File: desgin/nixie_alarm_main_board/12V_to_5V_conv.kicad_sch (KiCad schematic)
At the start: 8 parts

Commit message: filter caps
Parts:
- added C5: 100nF 25V, GRM033D70J224ME01D, symbol SamacSys_Parts:GRM033R71E101KA01J
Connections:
- net +12V: now also C5.1
- net GND: now also C5.2
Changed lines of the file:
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@@
+	)
+	(junction
+		(at 85.09 73.152)
+		(diameter 0)
+		(color 0 0 0 0)
 	)
 	(junction
@@
 	(wire
 		(pts
-			(xy 94.742 73.152) (xy 101.854 73.152)
+			(xy 74.676 73.152) (xy 85.09 73.152)
 		)
 		(stroke
@@
 	(wire
 		(pts
+			(xy 85.09 75.438) (xy 85.09 73.152)
+		)
+		(stroke
+			(width 0)
+			(type default)
+		)
+	)
+	(wire
+		(pts
 			(xy 191.516 91.44) (xy 191.516 108.458)
 		)
@@
 		(pts
 			(xy 125.984 83.82) (xy 139.7 83.82)
+		)
+		(stroke
+			(width 0)
+			(type default)
+		)
+	)
+	(wire
+		(pts
+			(xy 85.09 73.152) (xy 101.854 73.152)
 		)
 		(stroke
@@
 	(hierarchical_label "+12V"
 		(shape input)
-		(at 94.742 73.152 180)
+		(at 74.676 73.152 180)
 		(fields_autoplaced yes)
 		(effects
@@
 		(fields_autoplaced yes)
 		(property "Reference" "R6"
-			(at 104.394 99.3139 90)
+			(at 104.14 99.3139 90)
 			(effects
 				(font
@@
 		)
 		(property "Value" "15kΩ"
-			(at 104.394 101.8539 90)
+			(at 104.14 101.8539 90)
 			(effects
 				(font
@@
 					(unit 1)
 				)
+			)
+		)
+	)
+	(symbol
+		(lib_id "power:GND")
+		(at 85.09 88.138 0)
+		(unit 1)
+		(exclude_from_sim no)
+		(in_bom yes)
+		(on_board yes)
+		(dnp no)
+		(fields_autoplaced yes)
+		(property "Reference" "#PWR017"
+			(at 85.09 94.488 0)
+			(effects
+				(font
+					(size 1.27 1.27)
+				)
+				(hide yes)
+			)
+		)
+		(property "Value" "GND"
+			(at 85.09 92.71 0)
+			(effects
+				(font
+					(size 1.27 1.27)
+				)
+			)
+		)
+		(property "Footprint" ""
+			(at 85.09 88.138 0)
+			(effects
+				(font
+					(size 1.27 1.27)
+				)
+				(hide yes)
+			)
+		)
+		(property "Datasheet" ""
+			(at 85.09 88.138 0)
+			(effects
+				(font
+					(size 1.27 1.27)
+				)
+				(hide yes)
+			)
+		)
+		(property "Description" "Power symbol creates a global label with name \"GND\" , ground"
+			(at 85.09 88.138 0)
+			(effects
+				(font
+					(size 1.27 1.27)
+				)
+				(hide yes)
+			)
+		)
+		(pin "1"
+		)
+		(instances
+			(project "nixie_alarm_main_board"
+				(path "/a0d555d7-39a0-4a98-b831-70d97d0aa5a1/0943c442-6dd2-4b0d-a6a3-5c379f0041bb"
+					(reference "#PWR017")
+					(unit 1)
+				)
+			)
+		)
+	)
+	(symbol
+		(lib_id "SamacSys_Parts:GRM033R71E101KA01J")
+		(at 85.09 75.438 270)
+		(unit 1)
+		(exclude_from_sim no)
+		(in_bom yes)
+		(on_board yes)
+		(dnp no)
+		(property "Reference" "C5"
+			(at 90.678 79.756 90)
+			(effects
+				(font
+					(size 1.27 1.27)
+				)
+				(justify right)
+			)
+		)
+		(property "Value" "100nF 25V"
+			(at 98.552 81.788 90)
+			(effects
+				(font
+					(size 1.27 1.27)
+				)
+				(justify right)
+			)
+		)
+		(property "Footprint" "GRM033D70J224ME01D"
+			(at -11.1 84.328 0)
+			(effects
+				(font
+					(size 1.27 1.27)
+				)
+				(justify left top)
+				(hide yes)
+			)
+		)
+		(property "Datasheet" "https://search.murata.co.jp/Ceramy/image/img/A01X/G101/ENG/GRM033R71E101KA01-01A.pdf"
+			(at -111.1 84.328 0)
+			(effects
+				(font
+					(size 1.27 1.27)
+				)
+				(justify left top)
+				(hide yes)
+			)
+		)
+		(property "Description" "Multilayer Ceramic Capacitors MLCC - SMD/SMT 100pF 25 volts 10%"
+			(at 85.09 75.438 0)
+			(effects
+				(font
+					(size 1.27 1.27)
+				)
+				(hide yes)
+			)
+		)
+		(property "Height" "0.5"
+			(at -311.1 84.328 0)
+			(effects
+				(font
+					(size 1.27 1.27)
+				)
+				(justify left top)
+				(hide yes)
+			)
+		)
+		(property "Mouser Part Number" "81-GRM033R71E101KA1J"
+			(at -411.1 84.328 0)
+			(effects
+				(font
+					(size 1.27 1.27)
+				)
+				(justify left top)
+				(hide yes)
+			)
+		)
+		(property "Mouser Price/Stock" "https://www.mouser.co.uk/ProductDetail/Murata-Electronics/GRM033R71E101KA01J?qs=563MOeNa05Lmru4oTW10Jw%3D%3D"
+			(at -511.1 84.328 0)
+			(effects
+				(font
+					(size 1.27 1.27)
+				)
+				(justify left top)
+				(hide yes)
+			)
+		)
+		(property "Manufacturer_Name" "Murata Electronics"
+			(at -611.1 84.328 0)
+			(effects
+				(font
+					(size 1.27 1.27)
+				)
+				(justify left top)
+				(hide yes)
+			)
+		)
+		(property "Manufacturer_Part_Number" "GRM033R71E101KA01J"
+			(at -711.1 84.328 0)
+			(effects
+				(font
+					(size 1.27 1.27)
+				)
+				(justify left top)
+				(hide yes)
+			)
+		)
+		(pin "1"
+		)
+		(pin "2"
+		)
+		(instances
+			(project "nixie_alarm_main_board"
+				(path "/a0d555d7-39a0-4a98-b831-70d97d0aa5a1/0943c442-6dd2-4b0d-a6a3-5c379f0041bb"
+					(reference "C5")
+					(unit 1)
+				)

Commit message: new rezistors
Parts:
- C3, C5: footprint GRM033D70J224ME01D -> Capacitor_SMD:C_0805_2012Metric_Pad1.18x1.45mm_HandSolder
- R1, R2, R5, R6: footprint ERJUP6 -> Resistor_SMD:R_0805_2012Metric_Pad1.20x1.40mm_HandSolder
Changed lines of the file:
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@@
 			)
 		)
-		(property "Footprint" "ERJUP6"
+		(property "Footprint" "Resistor_SMD:R_0805_2012Metric_Pad1.20x1.40mm_HandSolder"
 			(at 5.664 87.122 0)
 			(effects
@@
 			)
 		)
-		(property "Footprint" "ERJUP6"
+		(property "Footprint" "Resistor_SMD:R_0805_2012Metric_Pad1.20x1.40mm_HandSolder"
 			(at 61.036 104.648 0)
 			(effects
@@
 			)
 		)
-		(property "Footprint" "ERJUP6"
+		(property "Footprint" "Resistor_SMD:R_0805_2012Metric_Pad1.20x1.40mm_HandSolder"
 			(at 61.036 77.47 0)
 			(effects
@@
 			)
 		)
-		(property "Footprint" "ERJUP6"
+		(property "Footprint" "Resistor_SMD:R_0805_2012Metric_Pad1.20x1.40mm_HandSolder"
 			(at 5.664 105.664 0)
 			(effects
@@
 			)
 		)
-		(property "Footprint" "GRM033D70J224ME01D"
+		(property "Footprint" "Capacitor_SMD:C_0805_2012Metric_Pad1.18x1.45mm_HandSolder"
 			(at -11.1 84.328 0)
 			(effects
@@
 			)
 		)
-		(property "Footprint" "GRM033D70J224ME01D"
+		(property "Footprint" "Capacitor_SMD:C_0805_2012Metric_Pad1.18x1.45mm_HandSolder"
 			(at 287.706 82.55 0)
 			(effects

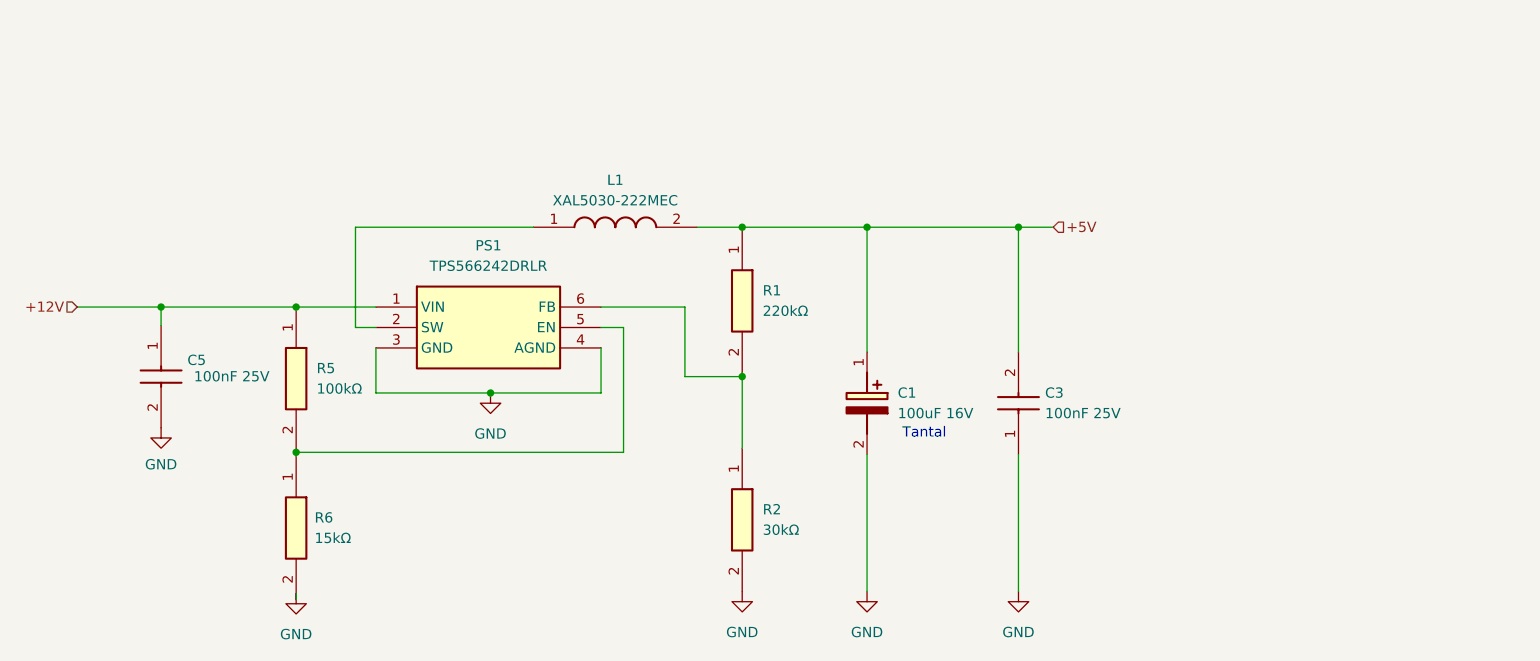
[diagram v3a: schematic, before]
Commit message: traces for nixie tubes
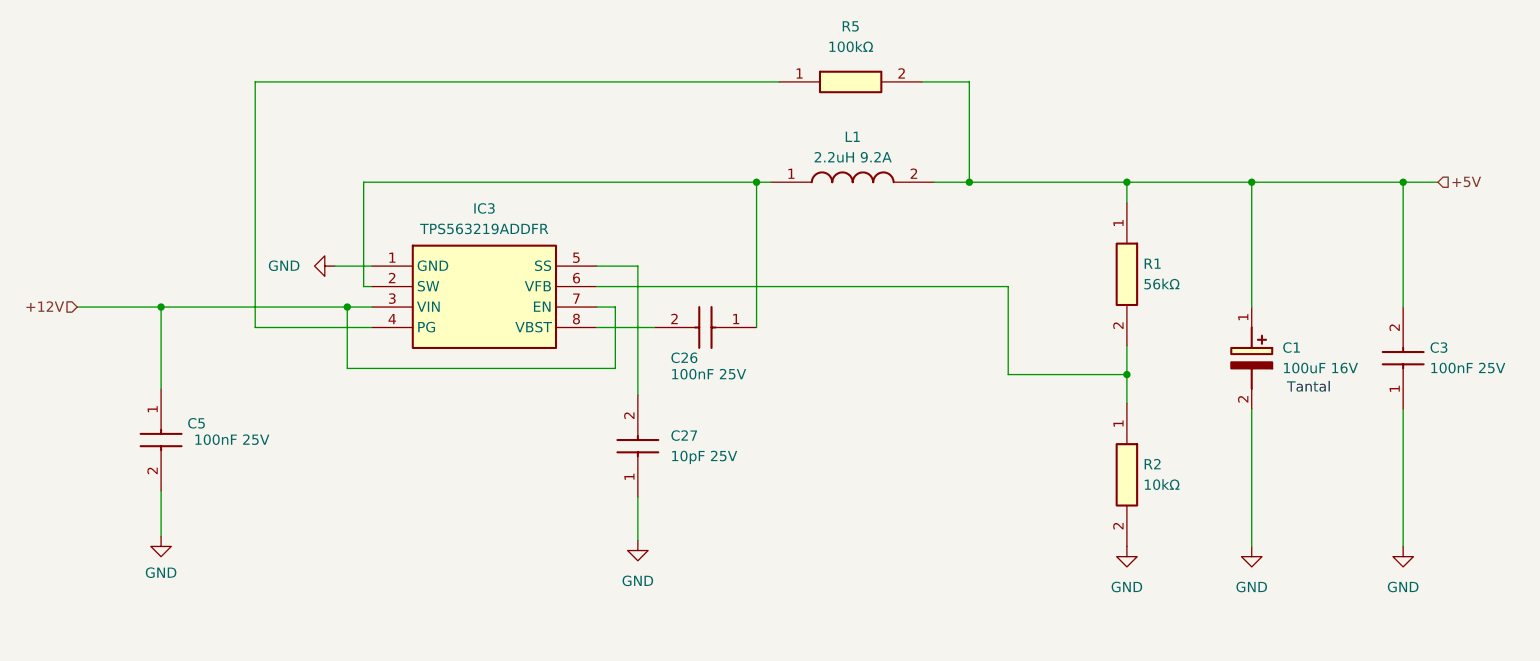
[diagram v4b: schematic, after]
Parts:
- removed PS1: TPS566242DRLR, SOT50P160X60-6N, symbol SamacSys_Parts:TPS566242DRLR
- removed R6: 15kΩ, Resistor_SMD:R_0805_2012Metric_Pad1.20x1.40mm_HandSolder, symbol SamacSys_Parts:ERJ-UP6D5101V
- added C26: 100nF 25V, Capacitor_SMD:C_0805_2012Metric_Pad1.18x1.45mm_HandSolder, symbol SamacSys_Parts:GRM033R71E101KA01J
- added C27: 10pF 25V, Capacitor_SMD:C_0805_2012Metric_Pad1.18x1.45mm_HandSolder, symbol SamacSys_Parts:GRM033R71E101KA01J
- added IC3: TPS563219ADDFR, SOT65P280X110-8N, symbol SamacSys_Parts:TPS563219ADDFR
- L1: value XAL5030-222MEC -> 2.2uH 9.2A
- R1: value 220kΩ -> 56kΩ
- R2: value 30kΩ -> 10kΩ
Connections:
- net +12V: now also IC3.3 (VIN), IC3.7 (EN); no longer R5.1
- net +5V: now also R5.2
- net GND: now also C27.1, IC3.1 (GND)
- net at L1.1: now also C26.1, IC3.2 (SW)
- net at R1.2, R2.1: now also IC3.6 (VFB)
- new net: IC3.4 (PG), R5.1
- new net: C27.2, IC3.5 (SS)
- new net: C26.2, IC3.8 (VBST)
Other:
- moved on the sheet: C1, C3, C5, L1, R1, R2, R5

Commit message: hv section
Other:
- moved on the sheet: C26
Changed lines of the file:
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@@
 	)
 	(junction
-		(at 159.004 57.658)
+		(at 154.94 57.658)
 		(diameter 0)
 		(color 0 0 0 0)
@@
 	(wire
 		(pts
-			(xy 110.236 57.658) (xy 159.004 57.658)
+			(xy 110.236 57.658) (xy 154.94 57.658)
 		)
 		(stroke
@@
 	(wire
 		(pts
-			(xy 159.004 57.658) (xy 159.004 75.692)
+			(xy 154.94 57.658) (xy 154.94 80.772)
 		)
 		(stroke
@@
 	(wire
 		(pts
+			(xy 141.986 75.692) (xy 139.192 75.692)
+		)
+		(stroke
+			(width 0)
+			(type default)
+		)
+	)
+	(wire
+		(pts
 			(xy 185.42 45.212) (xy 185.42 57.658)
 		)
@@
 	(wire
 		(pts
-			(xy 139.192 75.692) (xy 146.304 75.692)
+			(xy 141.986 80.772) (xy 142.24 80.772)
 		)
 		(stroke
@@
 	(wire
 		(pts
+			(xy 141.986 80.772) (xy 141.986 75.692)
+		)
+		(stroke
+			(width 0)
+			(type default)
+		)
+	)
+	(wire
+		(pts
 			(xy 108.204 73.152) (xy 111.252 73.152)
 		)
@@
 	(wire
 		(pts
+			(xy 154.94 57.658) (xy 160.782 57.658)
+		)
+		(stroke
+			(width 0)
+			(type default)
+		)
+	)
+	(wire
+		(pts
 			(xy 144.272 96.774) (xy 144.272 102.108)
 		)
@@
 		(pts
 			(xy 144.272 84.074) (xy 144.272 68.072)
-		)
-		(stroke
-			(width 0)
-			(type default)
-		)
-	)
-	(wire
-		(pts
-			(xy 159.004 57.658) (xy 160.782 57.658)
 		)
 		(stroke
@@
 	(symbol
 		(lib_id "SamacSys_Parts:GRM033R71E101KA01J")
-		(at 159.004 75.692 180)
+		(at 154.94 80.772 180)
 		(unit 1)
 		(exclude_from_sim no)
@@
 		(dnp no)
 		(property "Reference" "C26"
-			(at 148.336 79.502 0)
+			(at 144.272 84.582 0)
 			(effects
 				(font
@@
 		)
 		(property "Value" "100nF 25V"
-			(at 148.336 81.534 0)
+			(at 144.272 86.614 0)
 			(effects
 				(font
@@
 		)
 		(property "Footprint" "Capacitor_SMD:C_0805_2012Metric_Pad1.18x1.45mm_HandSolder"
-			(at 150.114 -20.498 0)
+			(at 146.05 -15.418 0)
 			(effects
 				(font
@@
 		)
 		(property "Datasheet" "https://search.murata.co.jp/Ceramy/image/img/A01X/G101/ENG/GRM033R71E101KA01-01A.pdf"
-			(at 150.114 -120.498 0)
+			(at 146.05 -115.418 0)
 			(effects
 				(font
@@
 		)
 		(property "Description" "Multilayer Ceramic Capacitors MLCC - SMD/SMT 100pF 25 volts 10%"
-			(at 159.004 75.692 0)
+			(at 154.94 80.772 0)
 			(effects
 				(font
@@
 		)
 		(property "Height" "0.5"
-			(at 150.114 -320.498 0)
+			(at 146.05 -315.418 0)
 			(effects
 				(font
@@
 		)
 		(property "Mouser Part Number" "81-GRM033R71E101KA1J"
-			(at 150.114 -420.498 0)
+			(at 146.05 -415.418 0)
 			(effects
 				(font
@@
 		)
 		(property "Mouser Price/Stock" "https://www.mouser.co.uk/ProductDetail/Murata-Electronics/GRM033R71E101KA01J?qs=563MOeNa05Lmru4oTW10Jw%3D%3D"
-			(at 150.114 -520.498 0)
+			(at 146.05 -515.418 0)
 			(effects
 				(font
@@
 		)
 		(property "Manufacturer_Name" "Murata Electronics"
-			(at 150.114 -620.498 0)
+			(at 146.05 -615.418 0)
 			(effects
 				(font
@@
 		)
 		(property "Manufacturer_Part_Number" "GRM033R71E101KA01J"
-			(at 150.114 -720.498 0)
-			(effects
-				(font
+			(at 146.05 -715.418 0)
+			(effects
+				(font

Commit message: little fixes
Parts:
- removed L1: 2.2uH 9.2A, XAL5030222MEC, symbol SamacSys_Parts:XAL5030-222MEC
- added L1: 2.2uH 9.7A, SRP5030CA4R7M, symbol SamacSys_Parts:SRP5030CA-2R2M
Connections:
- net +5V: now also L1.2
- net at C26.1, IC3.2 (SW): now also L1.1
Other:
- moved on the sheet: C26, C27

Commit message: fixes added
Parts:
- removed R5: 100kΩ, Resistor_SMD:R_0805_2012Metric_Pad1.20x1.40mm_HandSolder, symbol SamacSys_Parts:ERJ-UP6D5101V
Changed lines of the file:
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@@
-	)
-	(junction
-		(at 185.42 57.658)
-		(diameter 0)
-		(color 0 0 0 0)
 	)
 	(junction
@@
 	(wire
 		(pts
-			(xy 96.774 75.692) (xy 96.774 45.212)
-		)
-		(stroke
-			(width 0)
-			(type default)
-		)
-	)
-	(wire
-		(pts
 			(xy 85.09 83.312) (xy 85.09 73.152)
 		)
@@
 	(wire
 		(pts
-			(xy 183.134 57.658) (xy 185.42 57.658)
+			(xy 183.134 57.658) (xy 204.978 57.658)
 		)
 		(stroke
@@
 	(wire
 		(pts
-			(xy 111.252 75.692) (xy 96.774 75.692)
-		)
-		(stroke
-			(width 0)
-			(type default)
-		)
-	)
-	(wire
-		(pts
 			(xy 239.268 57.658) (xy 220.472 57.658)
 		)
@@
 	(wire
 		(pts
-			(xy 96.774 45.212) (xy 161.798 45.212)
-		)
-		(stroke
-			(width 0)
-			(type default)
-		)
-	)
-	(wire
-		(pts
 			(xy 220.472 57.658) (xy 220.472 73.152)
 		)
@@
 	(wire
 		(pts
-			(xy 179.578 45.212) (xy 185.42 45.212)
-		)
-		(stroke
-			(width 0)
-			(type default)
-		)
-	)
-	(wire
-		(pts
 			(xy 139.192 70.612) (xy 190.246 70.612)
 		)
@@
 	(wire
 		(pts
-			(xy 185.42 45.212) (xy 185.42 57.658)
-		)
-		(stroke
-			(width 0)
-			(type default)
-		)
-	)
-	(wire
-		(pts
 			(xy 146.812 81.026) (xy 147.828 81.026)
 		)
@@
 		(pts
 			(xy 110.236 57.658) (xy 110.236 70.612)
-		)
-		(stroke
-			(width 0)
-			(type default)
-		)
-	)
-	(wire
-		(pts
-			(xy 185.42 57.658) (xy 204.978 57.658)
 		)
 		(stroke
@@
 		)
 	)
-	(symbol
-		(lib_id "SamacSys_Parts:ERJ-UP6D5101V")
-		(at 161.798 45.212 0)
-		(unit 1)
-		(exclude_from_sim no)
-		(in_bom yes)
-		(on_board yes)
-		(dnp no)
-		(fields_autoplaced yes)
-		(property "Reference" "R5"
-			(at 170.688 38.354 0)
-			(effects
-				(font
-					(size 1.27 1.27)
-				)
-			)
-		)
-		(property "Value" "100kΩ"
-			(at 170.688 40.894 0)
-			(effects
-				(font
-					(size 1.27 1.27)
-				)
-			)
-		)
-		(property "Footprint" "Resistor_SMD:R_0805_2012Metric_Pad1.20x1.40mm_HandSolder"
-			(at 175.768 141.402 0)
-			(effects
-				(font
-					(size 1.27 1.27)
-				)
-				(justify left top)
-				(hide yes)
-			)
-		)
-		(property "Datasheet" "https://industrial.panasonic.com/cdbs/www-data/pdf/RDP0000/AOA0000C337.pdf"
-			(at 175.768 241.402 0)
-			(effects
-				(font
-					(size 1.27 1.27)
-				)
-				(justify left top)
-				(hide yes)
-			)
-		)
-		(property "Description" "Anti-Sulfurated Thick Film Chip Resistors/ Anti-Surge Type, Power Rating (W): 0.5, Chip Size (LxW(EIA)) (mm): 2.0 x 1.25 (EIA:0805), Resistance Values (?): 5100, Resistance Tolerance (%): 0.5, T.C.R (?102/K): ?100"
-			(at 161.798 45.212 0)
-			(effects
-				(font
-					(size 1.27 1.27)
-				)
-				(hide yes)
-			)
-		)
-		(property "Height" "0.7"
-			(at 175.768 441.402 0)
-			(effects
-				(font
-					(size 1.27 1.27)
-				)
-				(justify left top)
-				(hide yes)
-			)
-		)
-		(property "Mouser Part Number" "667-ERJ-UP6D5101V"
-			(at 175.768 541.402 0)
-			(effects
-				(font
-					(size 1.27 1.27)
-				)
-				(justify left top)
-				(hide yes)
-			)
-		)
-		(property "Mouser Price/Stock" "https://www.mouser.co.uk/ProductDetail/Panasonic/ERJ-UP6D5101V?qs=ZcfC38r4Pouz7%2FLHthUDHQ%3D%3D"
-			(at 175.768 641.402 0)
-			(effects
-				(font
-					(size 1.27 1.27)
-				)
-				(justify left top)
-				(hide yes)
-			)
-		)
-		(property "Manufacturer_Name" "Panasonic"
-			(at 175.768 741.402 0)
-			(effects
-				(font
-					(size 1.27 1.27)
-				)
-				(justify left top)
-				(hide yes)
-			)
-		)
-		(property "Manufacturer_Part_Number" "ERJ-UP6D5101V"
-			(at 175.768 841.402 0)
-			(effects
-				(font
-					(size 1.27 1.27)
-				)
-				(justify left top)
-				(hide yes)
-			)
-		)
-		(pin "1"
-		)
-		(pin "2"
-		)
-		(instances
-			(project "nixie_alarm_main_board"
-				(path "/a0d555d7-39a0-4a98-b831-70d97d0aa5a1/0943c442-6dd2-4b0d-a6a3-5c379f0041bb"
-					(reference "R5")
-					(unit 1)
-				)
-			)
-		)
-	)
